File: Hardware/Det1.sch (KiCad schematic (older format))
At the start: 46 parts

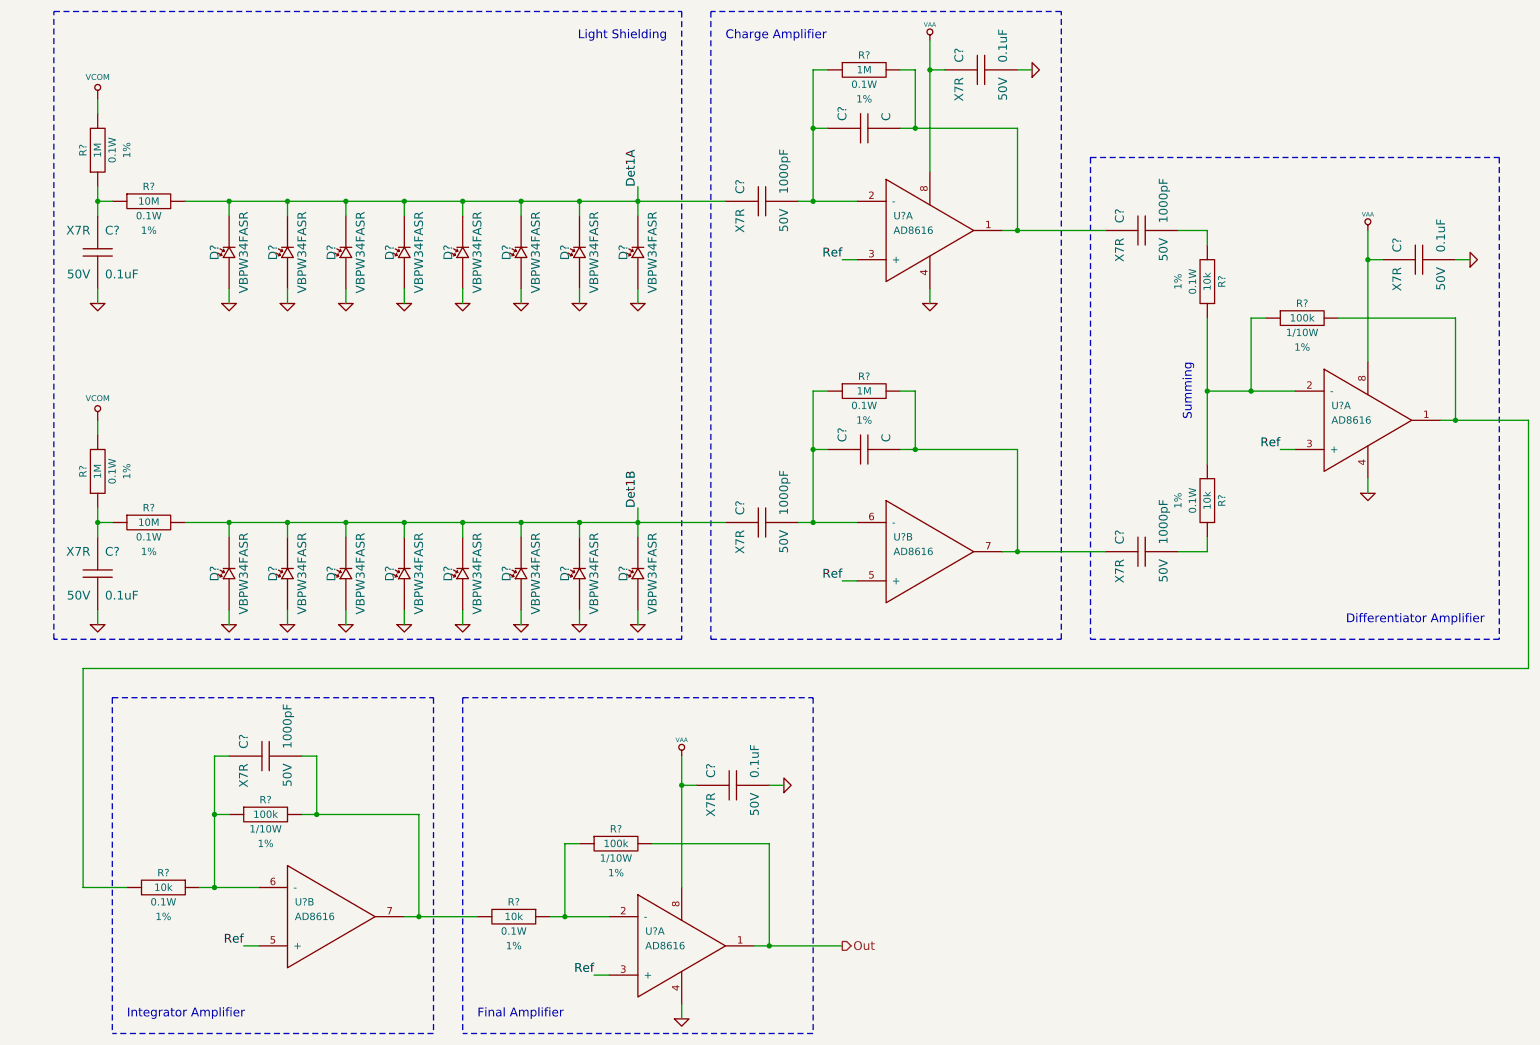
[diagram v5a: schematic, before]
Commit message: Rough layout for pin map testing
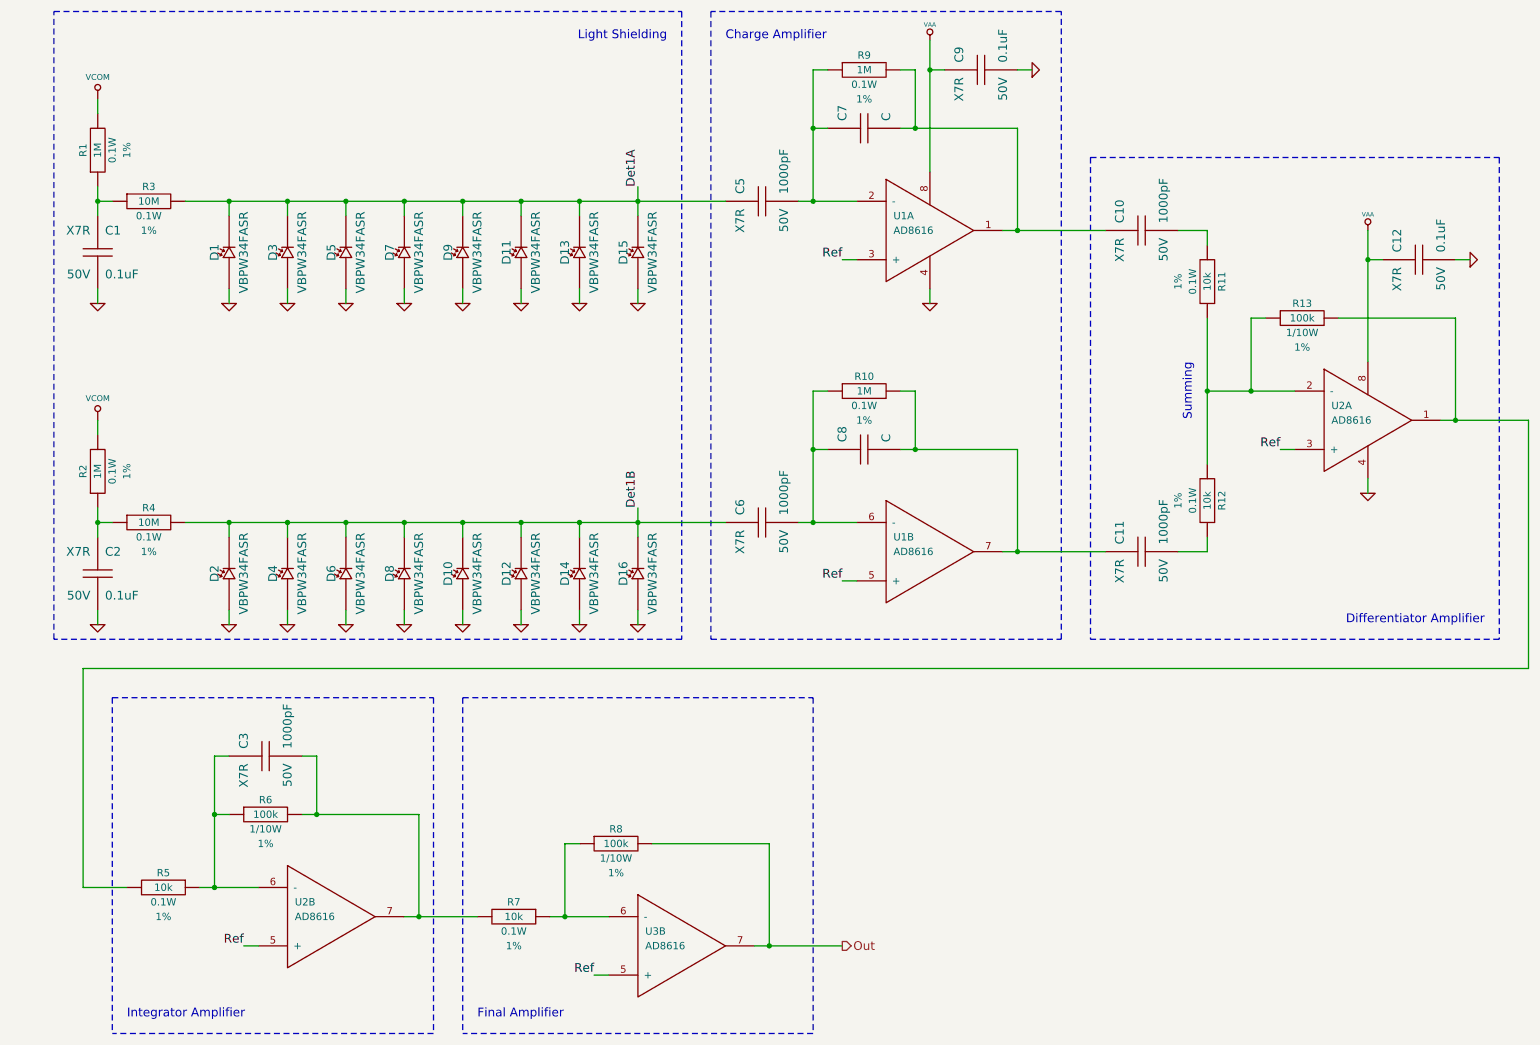
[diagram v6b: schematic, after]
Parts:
- removed C?: 0.1uF, CAPC1608, symbol C
- gave numbers to parts that had none: 43
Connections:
- net GND: now also U1.4; no longer U1.4, U3.4
- net Out: now also U3.7; no longer U1.1
- net Ref: now also U1.3 (+), U1.5 (+), U3.5 (+); no longer U1.3 (+), U1.5 (+), U3.3 (+)
- net VAA: now also U1.8; no longer U1.8, U3.8
- net at C5.2, C7.1, R9.1: now also U1.2 (-); no longer U2.2 (-)
- net at C10.1, C7.2, R9.2: now also U1.1; no longer U2.1
- net at C6.2, C8.1, R10.1: now also U1.6 (-); no longer U2.6 (-)
- net at C11.1, C8.2, R10.2: now also U1.7; no longer U2.7
- net at R11.1, R12.2, R13.1: now also U2.2 (-); no longer U3.2 (-)
- net at R13.2, R5.2: now also U2.1; no longer U3.1
- net at C3.1, R5.1, R6.1: now also U2.6 (-); no longer U1.6 (-)
- net at C3.2, R6.2, R7.2: now also U2.7; no longer U1.7
- net at R7.1, R8.1: now also U3.6 (-); no longer U1.2 (-)
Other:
- moved on the sheet: U2A, U2B

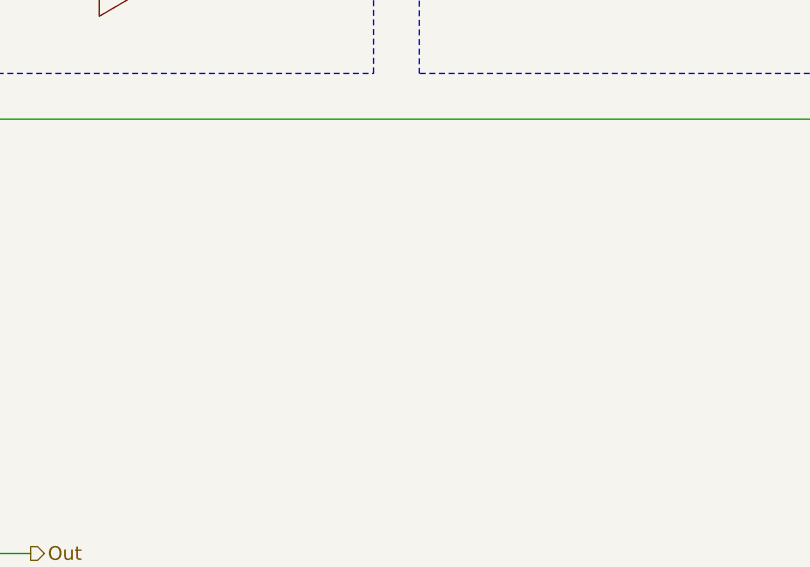
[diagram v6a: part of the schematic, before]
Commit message: Add opamp reference voltage
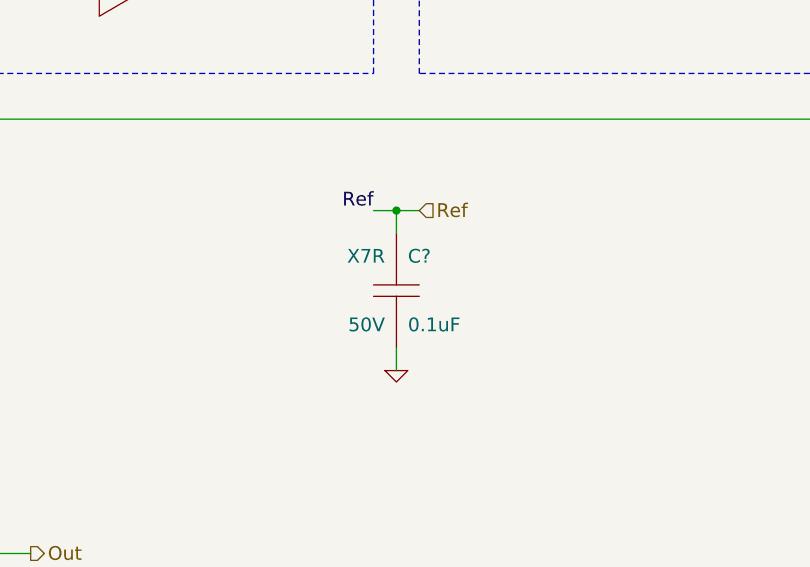
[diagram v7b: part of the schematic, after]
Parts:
- added C?: 0.1uF, CAPC1608, symbol C
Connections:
- net GND: now also C?.2
- net Ref: now also C?.1
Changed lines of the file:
@@
 Sheet 2 5
 Title "Solid State Cosmic Ray Detector"
-Date "28 sep 2014"
+Date "29 sep 2014"
 Rev "1"
 Comp "Ethan Harstad"
@@
 	0    -1   -1   0
 $EndComp
+Text HLabel 7700 5500 2    60   Input ~ 0
+Ref
+$Comp
+L C C?
+U 1 1 5429D051
+P 7600 5850
+F 0 "C?" H 7650 6000 60  0000 L CNN
+F 1 "0.1uF" H 7650 5700 60  0000 L CNN
+F 2 "CAPC1608" H 7600 5850 60  0001 C CNN
+F 3 "~" H 7600 5850 60  0000 C CNN
+F 4 "Samsung" H 7600 5850 60  0001 C CNN "MFR Name"
+F 5 "CL10B104KB8SFNC" H 7600 5850 60  0001 C CNN "MFR Part No"
+F 6 "1276-1936-1-ND" H 7600 5850 60  0001 C CNN "Distributor Part No"
+F 7 "50V" H 7550 5700 60  0000 R CNN "Voltage"
+F 8 "X7R" H 7550 6000 60  0000 R CNN "Dielectric"
+	1    7600 5850
+	1    0    0    -1
+$EndComp
+Text Label 7500 5500 2    60   ~ 0
+Ref
+Wire Wire Line
+	7500 5500 7700 5500
+Wire Wire Line
+	7600 5600 7600 5500
+Connection ~ 7600 5500
+$Comp
+L GND #PWR?
+U 1 1 5429D19C
+P 7600 6200
+F 0 "#PWR?" H 7600 6200 30  0001 C CNN
+F 1 "GND" H 7600 6130 30  0001 C CNN
+F 2 "" H 7600 6200 60  0000 C CNN
+F 3 "" H 7600 6200 60  0000 C CNN
+	1    7600 6200
+	1    0    0    -1
+$EndComp
+Wire Wire Line
+	7600 6200 7600 6100
 $EndSCHEMATC

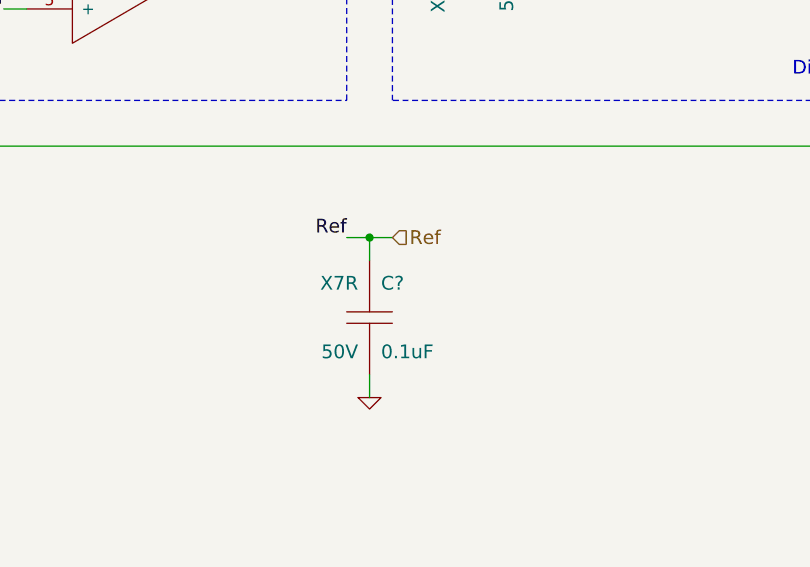
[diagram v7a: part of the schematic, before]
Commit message: Change comparator label for better routing
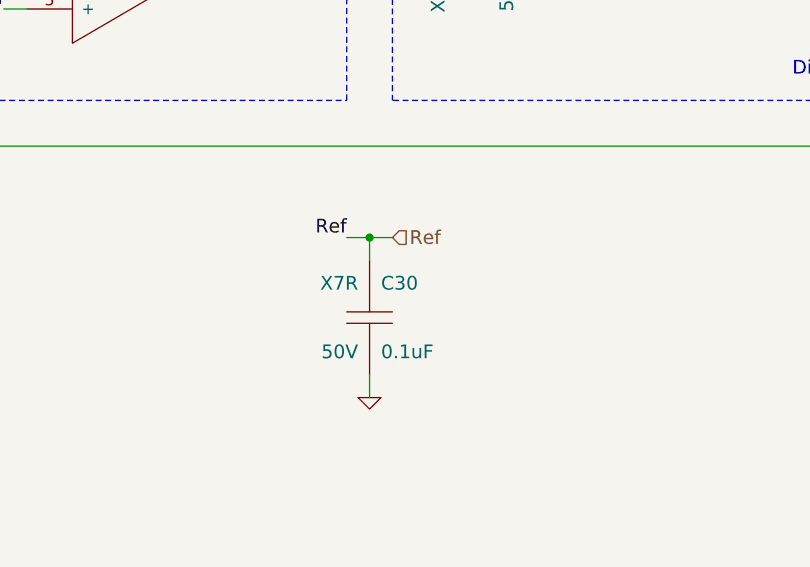
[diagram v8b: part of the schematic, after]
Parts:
- gave numbers to parts that had none: 1
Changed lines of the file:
@@
 $EndDescr
 $Comp
-L GND #PWR02
+L GND #PWR04
 U 1 1 523D026F
 P 1800 2600
-F 0 "#PWR02" H 1800 2600 30  0001 C CNN
+F 0 "#PWR04" H 1800 2600 30  0001 C CNN
 F 1 "GND" H 1800 2530 30  0001 C CNN
 F 2 "" H 1800 2600 60  0000 C CNN
@@
 $EndComp
 $Comp
-L GND #PWR03
+L GND #PWR05
 U 1 1 523D027E
 P 2200 2600
-F 0 "#PWR03" H 2200 2600 30  0001 C CNN
+F 0 "#PWR05" H 2200 2600 30  0001 C CNN
 F 1 "GND" H 2200 2530 30  0001 C CNN
 F 2 "" H 2200 2600 60  0000 C CNN
@@
 $EndComp
 $Comp
-L GND #PWR04
+L GND #PWR06
 U 1 1 523D029C
 P 3000 2600
-F 0 "#PWR04" H 3000 2600 30  0001 C CNN
+F 0 "#PWR06" H 3000 2600 30  0001 C CNN
 F 1 "GND" H 3000 2530 30  0001 C CNN
 F 2 "" H 3000 2600 60  0000 C CNN
@@
 $EndComp
 $Comp
-L GND #PWR05
+L GND #PWR07
 U 1 1 523D02AB
 P 2600 2600
-F 0 "#PWR05" H 2600 2600 30  0001 C CNN
+F 0 "#PWR07" H 2600 2600 30  0001 C CNN
 F 1 "GND" H 2600 2530 30  0001 C CNN
 F 2 "" H 2600 2600 60  0000 C CNN
@@
 $EndComp
 $Comp
-L GND #PWR06
+L GND #PWR08
 U 1 1 523D1DB5
 P 900 2600
-F 0 "#PWR06" H 900 2600 30  0001 C CNN
+F 0 "#PWR08" H 900 2600 30  0001 C CNN
 F 1 "GND" H 900 2530 30  0001 C CNN
 F 2 "" H 900 2600 60  0000 C CNN
@@
 $EndComp
 $Comp
-L GND #PWR07
+L GND #PWR09
 U 1 1 52411FD2
 P 3400 2600
-F 0 "#PWR07" H 3400 2600 30  0001 C CNN
+F 0 "#PWR09" H 3400 2600 30  0001 C CNN
 F 1 "GND" H 3400 2530 30  0001 C CNN
 F 2 "" H 3400 2600 60  0000 C CNN
@@
 $EndComp
 $Comp
-L GND #PWR08
+L GND #PWR010
 U 1 1 52411FD8
 P 3800 2600
-F 0 "#PWR08" H 3800 2600 30  0001 C CNN
+F 0 "#PWR010" H 3800 2600 30  0001 C CNN
 F 1 "GND" H 3800 2530 30  0001 C CNN
 F 2 "" H 3800 2600 60  0000 C CNN
@@
 $EndComp
 $Comp
-L GND #PWR09
+L GND #PWR011
 U 1 1 52411FDE
 P 4600 2600
-F 0 "#PWR09" H 4600 2600 30  0001 C CNN
+F 0 "#PWR011" H 4600 2600 30  0001 C CNN
 F 1 "GND" H 4600 2530 30  0001 C CNN
 F 2 "" H 4600 2600 60  0000 C CNN
@@
 $EndComp
 $Comp
-L GND #PWR010
+L GND #PWR012
 U 1 1 52411FE4
 P 4200 2600
-F 0 "#PWR010" H 4200 2600 30  0001 C CNN
+F 0 "#PWR012" H 4200 2600 30  0001 C CNN
 F 1 "GND" H 4200 2530 30  0001 C CNN
 F 2 "" H 4200 2600 60  0000 C CNN
@@
 $EndComp
 $Comp
-L GND #PWR011
+L GND #PWR013
 U 1 1 52B68909
 P 1800 4800
-F 0 "#PWR011" H 1800 4800 30  0001 C CNN
+F 0 "#PWR013" H 1800 4800 30  0001 C CNN
 F 1 "GND" H 1800 4730 30  0001 C CNN
 F 2 "" H 1800 4800 60  0000 C CNN
@@
 $EndComp
 $Comp
-L GND #PWR012
+L GND #PWR014
 U 1 1 52B6890F
 P 2200 4800
-F 0 "#PWR012" H 2200 4800 30  0001 C CNN
+F 0 "#PWR014" H 2200 4800 30  0001 C CNN
 F 1 "GND" H 2200 4730 30  0001 C CNN
 F 2 "" H 2200 4800 60  0000 C CNN
@@
 $EndComp
 $Comp
-L GND #PWR013
+L GND #PWR015
 U 1 1 52B68915
 P 3000 4800
-F 0 "#PWR013" H 3000 4800 30  0001 C CNN
+F 0 "#PWR015" H 3000 4800 30  0001 C CNN
 F 1 "GND" H 3000 4730 30  0001 C CNN
 F 2 "" H 3000 4800 60  0000 C CNN
@@
 $EndComp
 $Comp
-L GND #PWR014
+L GND #PWR016
 U 1 1 52B6891B
 P 2600 4800
-F 0 "#PWR014" H 2600 4800 30  0001 C CNN
+F 0 "#PWR016" H 2600 4800 30  0001 C CNN
 F 1 "GND" H 2600 4730 30  0001 C CNN
 F 2 "" H 2600 4800 60  0000 C CNN
@@
 $EndComp
 $Comp
-L GND #PWR015
+L GND #PWR017
 U 1 1 52B6892E
 P 3400 4800
-F 0 "#PWR015" H 3400 4800 30  0001 C CNN
+F 0 "#PWR017" H 3400 4800 30  0001 C CNN
 F 1 "GND" H 3400 4730 30  0001 C CNN
 F 2 "" H 3400 4800 60  0000 C CNN
@@
 $EndComp
 $Comp
-L GND #PWR016
+L GND #PWR018
 U 1 1 52B68934
 P 3800 4800
-F 0 "#PWR016" H 3800 4800 30  0001 C CNN
+F 0 "#PWR018" H 3800 4800 30  0001 C CNN
 F 1 "GND" H 3800 4730 30  0001 C CNN
 F 2 "" H 3800 4800 60  0000 C CNN
@@
 $EndComp
 $Comp
-L GND #PWR017
+L GND #PWR019
 U 1 1 52B6893A
 P 4600 4800
-F 0 "#PWR017" H 4600 4800 30  0001 C CNN
+F 0 "#PWR019" H 4600 4800 30  0001 C CNN
 F 1 "GND" H 4600 4730 30  0001 C CNN
 F 2 "" H 4600 4800 60  0000 C CNN
@@
 $EndComp
 $Comp
-L GND #PWR018
+L GND #PWR020
 U 1 1 52B68940
 P 4200 4800
-F 0 "#PWR018" H 4200 4800 30  0001 C CNN
+F 0 "#PWR020" H 4200 4800 30  0001 C CNN
 F 1 "GND" H 4200 4730 30  0001 C CNN
 F 2 "" H 4200 4800 60  0000 C CNN
@@
 $EndComp
 $Comp
-L GND #PWR019
+L GND #PWR021
 U 1 1 52BD5A4A
 P 900 4800
-F 0 "#PWR019" H 900 4800 30  0001 C CNN
+F 0 "#PWR021" H 900 4800 30  0001 C CNN
 F 1 "GND" H 900 4730 30  0001 C CNN
 F 2 "" H 900 4800 60  0000 C CNN
@@
 $EndComp
 $Comp
-L VCOM #PWR4
+L VCOM #PWR6
 U 1 1 5421E1E7
 P 900 3400
-F 0 "#PWR4" H 900 3600 40  0001 C CNN
+F 0 "#PWR6" H 900 3600 40  0001 C CNN
 F 1 "VCOM" H 900 3550 40  0000 C CNN
 F 2 "" H 900 3400 60  0000 C CNN
@@
 $EndComp
 $Comp
-L VCOM #PWR2
+L VCOM #PWR4
 U 1 1 5421E1F6
 P 900 1200
-F 0 "#PWR2" H 900 1400 40  0001 C CNN
+F 0 "#PWR4" H 900 1400 40  0001 C CNN
 F 1 "VCOM" H 900 1350 40  0000 C CNN
 F 2 "" H 900 1200 60  0000 C CNN
@@
 Connection ~ 6500 1400
 $Comp
-L VAA #PWR020
+L VAA #PWR022
 U 1 1 5421E452
 P 6600 800
-F 0 "#PWR020" H 6600 860 30  0001 C CNN
+F 0 "#PWR022" H 6600 860 30  0001 C CNN
 F 1 "VAA" H 6600 910 30  0000 C CNN
 F 2 "" H 6600 800 60  0000 C CNN
@@
 Connection ~ 6600 1000
 $Comp
-L GND #PWR021
+L GND #PWR023
 U 1 1 5421E4F4
 P 7300 1000
-F 0 "#PWR021" H 7300 1000 30  0001 C CNN
+F 0 "#PWR023" H 7300 1000 30  0001 C CNN
 F 1 "GND" H 7300 930 30  0001 C CNN
 F 2 "" H 7300 1000 60  0000 C CNN
@@
 	7300 1000 7200 1000
 $Comp
-L GND #PWR022
+L GND #PWR024
 U 1 1 5421E54F
 P 6600 2600
-F 0 "#PWR022" H 6600 2600 30  0001 C CNN
+F 0 "#PWR024" H 6600 2600 30  0001 C CNN
 F 1 "GND" H 6600 2530 30  0001 C CNN
 F 2 "" H 6600 2600 60  0000 C CNN
@@
 	8900 2700 8800 2700
 $Comp
-L VAA #PWR023
+L VAA #PWR025
 U 1 1 5421E7C8
 P 9600 2100
-F 0 "#PWR023" H 9600 2160 30  0001 C CNN
+F 0 "#PWR025" H 9600 2160 30  0001 C CNN
 F 1 "VAA" H 9600 2210 30  0000 C CNN
 F 2 "" H 9600 2100 60  0000 C CNN
@@
 Connection ~ 9600 2300
 $Comp
-L GND #PWR024
+L GND #PWR026
 U 1 1 5421E89D
 P 10300 2300
-F 0 "#PWR024" H 10300 2300 30  0001 C CNN
+F 0 "#PWR026" H 10300 2300 30  0001 C CNN
 F 1 "GND" H 10300 2230 30  0001 C CNN
 F 2 "" H 10300 2300 60  0000 C CNN
@@
 	1600 6600 2000 6600
 $Comp
-L GND #PWR025
+L GND #PWR027
 U 1 1 5421EC65
 P 9600 3900
-F 0 "#PWR025" H 9600 3900 30  0001 C CNN
+F 0 "#PWR027" H 9600 3900 30  0001 C CNN
 F 1 "GND" H 9600 3830 30  0001 C CNN
 F 2 "" H 9600 3900 60  0000 C CNN
@@
 Ref
 $Comp
-L C C?
+L C C30
 U 1 1 5429D051
 P 7600 5850
-F 0 "C?" H 7650 6000 60  0000 L CNN
+F 0 "C30" H 7650 6000 60  0000 L CNN
 F 1 "0.1uF" H 7650 5700 60  0000 L CNN
 F 2 "CAPC1608" H 7600 5850 60  0001 C CNN
@@
 Connection ~ 7600 5500
 $Comp
-L GND #PWR?
+L GND #PWR028
 U 1 1 5429D19C
 P 7600 6200
-F 0 "#PWR?" H 7600 6200 30  0001 C CNN
+F 0 "#PWR028" H 7600 6200 30  0001 C CNN
 F 1 "GND" H 7600 6130 30  0001 C CNN
 F 2 "" H 7600 6200 60  0000 C CNN
